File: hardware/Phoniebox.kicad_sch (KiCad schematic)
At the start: 71 parts, among them J1 GPIO, J2 Screw_Terminal_01x08, J3 Screw_Terminal_01x08, J4 Screw_Terminal_01x08, J5 Conn_01x02, J6 Conn_02x06_Odd_Even, J8 Conn_01x08, Q1 2N7002, Q2 2N7002, Q3 2N7002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

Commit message: Add OnOff-SHIM circuit to PCB
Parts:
- removed C1: 1n, Capacitor_SMD:C_0603_1608Metric_Pad1.08x0.95mm_HandSolder, symbol Device:C
- removed J5: Conn_01x02, Connector_PinHeader_2.54mm:PinHeader_1x02_P2.54mm_Vertical, symbol Connector_Generic:Conn_01x02
- removed J8: Conn_01x08, Connector_PinHeader_2.54mm:PinHeader_1x08_P2.54mm_Vertical, symbol Connector_Generic:Conn_01x08
- removed R1: 10k, Resistor_SMD:R_0603_1608Metric_Pad0.98x0.95mm_HandSolder, symbol Device:R
- removed R2: 100, Resistor_SMD:R_0603_1608Metric_Pad0.98x0.95mm_HandSolder, symbol Device:R
- added C21: 4u7, Capacitor_SMD:C_0603_1608Metric_Pad1.08x0.95mm_HandSolder, symbol Device:C
- added D1: BAT54C, Package_TO_SOT_SMD:SOT-23, symbol Diode:BAT54C
- added J7: USB_B_Micro, Connector_USB:USB_Micro-B_Amphenol_10118194_Horizontal, symbol Connector:USB_B_Micro
- added J8: Conn_02x04_Odd_Even, Connector_PinHeader_2.54mm:PinHeader_2x04_P2.54mm_Vertical_SMD, symbol Connector_Generic:Conn_02x04_Odd_Even
- added Q7: AO3401A, Package_TO_SOT_SMD:SOT-23, symbol Transistor_FET:AO3401A
- added Q8: 2N7002, Package_TO_SOT_SMD:SOT-23, symbol Transistor_FET:2N7002
- added R24: 100k, Resistor_SMD:R_0603_1608Metric_Pad0.98x0.95mm_HandSolder, symbol Device:R
- added R25: 10k, Resistor_SMD:R_0603_1608Metric_Pad0.98x0.95mm_HandSolder, symbol Device:R
- added R26, R27, R28: 1k, Resistor_SMD:R_0603_1608Metric_Pad0.98x0.95mm_HandSolder, symbol Device:R
- J6: footprint Connector_PinHeader_2.54mm:PinHeader_2x06_P2.54mm_Vertical -> Connector_PinHeader_2.54mm:PinHeader_2x06_P2.54mm_Vertical_SMD
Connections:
- net ~{MUTE} is gone; now on net GPIO2: U1.5 (~{MUTE})
- net +3V3: now also J8.1 (Pin_1), R26.2, R28.2
- net +5V: now also Q7.3 (D), R27.2
- net Button_1: now also D1.3, R25.1
- net GND: now also J4.1 (Pin_1), J4.4 (Pin_4), C21.2, J7.5 (GND), J7.6 (Shield), J8.3 (Pin_3), Q8.2 (S); no longer J4.3 (Pin_3), J4.6 (Pin_6)
- net GPIO2: no longer U1.12 (~{SHDN})
- net GPIO3: now also U1.12 (~{SHDN})
- net INL: now also J4.7 (Pin_7); no longer J4.1 (Pin_1)
- net INR: now also J4.8 (Pin_8); no longer J4.2 (Pin_2)
- net IRQ: now also J8.4 (Pin_4)
- net MISO: now also J8.5 (Pin_5)
- net MOSI: now also J8.6 (Pin_6)
- net Power_Cut: no longer J1.7 (Pin_7)
- net RST: now also J8.2 (Pin_2)
- net SCK: now also J8.7 (Pin_7)
- net SDA: now also J8.8 (Pin_8)
- net SPK_L+: now also J4.2 (Pin_2); no longer J4.4 (Pin_4)
- net SPK_L-: now also J4.3 (Pin_3); no longer J4.5 (Pin_5)
- net SPK_R+: now also J4.6 (Pin_6); no longer J4.8 (Pin_8)
- net SPK_R-: now also J4.5 (Pin_5); no longer J4.7 (Pin_7)
- net Trigger: no longer J1.11 (Pin_11)
- new net: D1.1, R27.1
- new net GPIO17_Trigger: D1.2, J1.11 (Pin_11), R28.1
- new net GPIO4_PowerOff: C21.1, J1.7 (Pin_7), Q8.1 (G), R26.1
- new net Q7_G: Q7.1 (G), Q8.3 (D), R24.1, R25.2
- new net VBUS: J7.1 (VBUS), Q7.2 (S), R24.2

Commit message: Fix DRC errors/warnings, Add round edges for PCB.
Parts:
- removed J6: Conn_02x06_Odd_Even, Connector_PinHeader_2.54mm:PinHeader_2x06_P2.54mm_Vertical_SMD, symbol Connector_Generic:Conn_02x06_Odd_Even
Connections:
- net +3V3: no longer J1.1 (Pin_1)
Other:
- note removed: "On/Off SHIM"
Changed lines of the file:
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@@
   (junction (at 130.81 81.28) (diameter 0) (color 0 0 0 0)
   )
-  (junction (at 144.78 29.21) (diameter 1.016) (color 0 0 0 0)
-  )
   (junction (at 207.01 143.51) (diameter 0) (color 0 0 0 0)
   )
@@
   (junction (at 119.38 102.87) (diameter 0) (color 0 0 0 0)
   )
-  (junction (at -78.74 21.59) (diameter 1.016) (color 0 0 0 0)
-  )
   (wire (pts (xy 411.48 135.89) (xy 420.37 135.89))
     (stroke (width 0) (type default) (color 0 0 0 0))
@@
     (stroke (width 0) (type solid) (color 0 0 0 0))
   )
-  (wire (pts (xy 144.78 31.75) (xy 142.24 31.75))
-    (stroke (width 0) (type solid) (color 0 0 0 0))
-  )
   (wire (pts (xy 252.73 25.4) (xy 273.05 25.4))
     (stroke (width 0) (type default) (color 0 0 0 0))
@@
     (stroke (width 0) (type solid) (color 0 0 0 0))
   )
-  (wire (pts (xy -78.74 17.78) (xy -78.74 21.59))
+  (wire (pts (xy -78.74 17.78) (xy -78.74 41.91))
     (stroke (width 0) (type solid) (color 0 0 0 0))
   )
-  (wire (pts (xy 111.76 36.83) (xy 129.54 36.83))
-    (stroke (width 0) (type default) (color 0 0 0 0))
-  )
   (wire (pts (xy 59.69 34.29) (xy 59.69 35.56))
     (stroke (width 0) (type default) (color 0 0 0 0))
@@
     (stroke (width 0) (type default) (color 0 0 0 0))
   )
-  (wire (pts (xy 124.46 39.37) (xy 124.46 45.72))
-    (stroke (width 0) (type default) (color 0 0 0 0))
-  )
   (wire (pts (xy -58.42 36.83) (xy -58.42 44.45))
     (stroke (width 0) (type solid) (color 0 0 0 0))
@@
     (stroke (width 0) (type default) (color 0 0 0 0))
   )
-  (wire (pts (xy 111.76 41.91) (xy 129.54 41.91))
-    (stroke (width 0) (type default) (color 0 0 0 0))
-  )
   (wire (pts (xy -58.42 17.78) (xy -58.42 21.59))
     (stroke (width 0) (type solid) (color 0 0 0 0))
@@
     (stroke (width 0) (type default) (color 0 0 0 0))
   )
-  (wire (pts (xy 142.24 34.29) (xy 144.78 34.29))
-    (stroke (width 0) (type default) (color 0 0 0 0))
-  )
   (wire (pts (xy 101.6 81.28) (xy 104.14 81.28))
     (stroke (width 0) (type default) (color 0 0 0 0))
@@
     (stroke (width 0) (type solid) (color 0 0 0 0))
   )
-  (wire (pts (xy -78.74 21.59) (xy -78.74 41.91))
-    (stroke (width 0) (type solid) (color 0 0 0 0))
-  )
   (wire (pts (xy 175.26 39.37) (xy 184.15 39.37))
     (stroke (width 0) (type default) (color 0 0 0 0))
@@
     (stroke (width 0) (type default) (color 0 0 0 0))
   )
-  (wire (pts (xy 144.78 29.21) (xy 144.78 31.75))
-    (stroke (width 0) (type solid) (color 0 0 0 0))
-  )
   (wire (pts (xy 373.38 44.45) (xy 373.38 41.91))
     (stroke (width 0) (type default) (color 0 0 0 0))
@@
     (stroke (width 0) (type default) (color 0 0 0 0))
   )
-  (wire (pts (xy 129.54 39.37) (xy 124.46 39.37))
-    (stroke (width 0) (type default) (color 0 0 0 0))
-  )
   (wire (pts (xy 153.67 101.6) (xy 153.67 102.87))
     (stroke (width 0) (type default) (color 0 0 0 0))
@@
     (stroke (width 0) (type default) (color 0 0 0 0))
   )
-  (wire (pts (xy 124.46 29.21) (xy 129.54 29.21))
-    (stroke (width 0) (type solid) (color 0 0 0 0))
-  )
   (wire (pts (xy 162.56 88.9) (xy 153.67 88.9))
     (stroke (width 0) (type default) (color 0 0 0 0))
@@
     (stroke (width 0) (type default) (color 0 0 0 0))
   )
-  (wire (pts (xy 144.78 25.4) (xy 144.78 29.21))
-    (stroke (width 0) (type solid) (color 0 0 0 0))
-  )
   (wire (pts (xy 207.01 146.05) (xy 207.01 143.51))
     (stroke (width 0) (type default) (color 0 0 0 0))
@@
     (stroke (width 0) (type default) (color 0 0 0 0))
   )
-  (wire (pts (xy 144.78 45.72) (xy 144.78 34.29))
-    (stroke (width 0) (type default) (color 0 0 0 0))
-  )
   (wire (pts (xy 403.86 135.89) (xy 401.32 135.89))
     (stroke (width 0) (type default) (color 0 0 0 0))
@@
     (stroke (width 0) (type solid) (color 0 0 0 0))
   )
-  (wire (pts (xy 144.78 29.21) (xy 142.24 29.21))
-    (stroke (width 0) (type solid) (color 0 0 0 0))
-  )
   (wire (pts (xy 219.71 27.94) (xy 231.14 27.94))
     (stroke (width 0) (type default) (color 0 0 0 0))
@@
     (stroke (width 0) (type default) (color 0 0 0 0))
   )
-  (wire (pts (xy -78.74 21.59) (xy -73.66 21.59))
-    (stroke (width 0) (type solid) (color 0 0 0 0))
-  )
   (wire (pts (xy 153.67 39.37) (xy 162.56 39.37))
     (stroke (width 0) (type default) (color 0 0 0 0))
@@
     (stroke (width 0) (type default) (color 0 0 0 0))
   )
-  (wire (pts (xy 124.46 25.4) (xy 124.46 29.21))
-    (stroke (width 0) (type solid) (color 0 0 0 0))
-  )
   (wire (pts (xy 481.33 105.41) (xy 478.79 105.41))
     (stroke (width 0) (type default) (color 0 0 0 0))
@@
     (stroke (width 0) (type default) (color 0 0 0 0))
   )
-  (text "On/Off SHIM" (at 130.81 19.05 0)
-    (effects (font (size 1.27 1.27)) (justify left bottom))
-  )
   (text "Buttons" (at 271.78 45.72 0)
     (effects (font (size 1.27 1.27)) (justify left bottom))
@@
     (effects (font (size 1.27 1.27)) (justify right bottom))
   )
-  (label "Power_Cut" (at 111.76 36.83 0)
-    (effects (font (size 1.27 1.27)) (justify left bottom))
-  )
   (label "GPIO12" (at -34.29 59.69 180)
     (effects (font (size 1.27 1.27)) (justify right bottom))
   )
-  (label "Trigger" (at 111.76 41.91 0)
-    (effects (font (size 1.27 1.27)) (justify left bottom))
-  )
   (label "LED_2" (at 453.39 105.41 0)
     (effects (font (size 1.27 1.27)) (justify left bottom))
@@
     (pin "2")
   )
-  (symbol (lib_id "power:+5V") (at 144.78 25.4 0) (unit 1)
-    (in_bom yes) (on_board yes)
-    (property "Reference" "#PWR0122" (id 0) (at 144.78 29.21 0)
-      (effects (font (size 1.27 1.27)) hide)
-    )
-    (property "Value" "+5V" (id 1) (at 145.1483 21.0756 0))
-    (property "Footprint" "" (id 2) (at 144.78 25.4 0))
-    (property "Datasheet" "" (id 3) (at 144.78 25.4 0))
-    (pin "1")
-  )
   (symbol (lib_id "Device:R") (at 115.57 135.89 180) (unit 1)
     (in_bom yes) (on_board yes) (fields_autoplaced)
@@
     (pin "1")
   )
-  (symbol (lib_id "power:+3.3V") (at 124.46 25.4 0) (unit 1)
-    (in_bom yes) (on_board yes)
-    (property "Reference" "#PWR0120" (id 0) (at 124.46 29.21 0)
-      (effects (font (size 1.27 1.27)) hide)
-    )
-    (property "Value" "+3.3V" (id 1) (at 124.8283 21.0756 0))
-    (property "Footprint" "" (id 2) (at 124.46 25.4 0))
-    (property "Datasheet" "" (id 3) (at 124.46 25.4 0))
-    (pin "1")
-  )
   (symbol (lib_id "power:+3.3VA") (at 358.14 41.91 0) (unit 1)
     (in_bom yes) (on_board yes) (fields_autoplaced)
@@
     (pin "1")
   )
-  (symbol (lib_id "Connector_Generic:Conn_02x06_Odd_Even") (at 134.62 34.29 0) (unit 1)
-    (in_bom yes) (on_board yes) (fields_autoplaced)
-    (property "Reference" "J6" (id 0) (at 135.89 25.4 0))
-    (property "Value" "Conn_02x06_Odd_Even" (id 1) (at 135.89 25.4 0)
-      (effects (font (size 1.27 1.27)) hide)
-    )
-    (property "Footprint" "Connector_PinHeader_2.54mm:PinHeader_2x06_P2.54mm_Vertical_SMD" (id 2) (at 134.62 34.29 0)
-      (effects (font (size 1.27 1.27)) hide)
-    )
-    (property "Datasheet" "~" (id 3) (at 134.62 34.29 0)
-      (effects (font (size 1.27 1.27)) hide)
-    )
-    (pin "1")
-    (pin "10")
-    (pin "11")
-    (pin "12")
-    (pin "2")
-    (pin "3")
-    (pin "4")
-    (pin "5")
-    (pin "6")
-    (pin "7")
-    (pin "8")
-    (pin "9")
-  )
   (symbol (lib_id "power:+5V") (at 313.69 15.24 0) (unit 1)
     (in_bom yes) (on_board yes)
@@
     (pin "1")
   )
-  (symbol (lib_id "power:GND") (at 144.78 45.72 0) (unit 1)
-    (in_bom yes) (on_board yes)
-    (property "Reference" "#PWR0124" (id 0) (at 144.78 52.07 0)
-      (effects (font (size 1.27 1.27)) hide)
-    )
-    (property "Value" "GND" (id 1) (at 144.8943 50.0444 0))
-    (property "Footprint" "" (id 2) (at 144.78 45.72 0))
-    (property "Datasheet" "" (id 3) (at 144.78 45.72 0))
-    (pin "1")
-  )
   (symbol (lib_id "power:GND") (at 401.32 152.4 0) (unit 1)
     (in_bom yes) (on_board yes)
@@
     (pin "2")
   )
-  (symbol (lib_id "power:GND") (at 124.46 45.72 0) (unit 1)
-    (in_bom yes) (on_board yes)
-    (property "Reference" "#PWR0123" (id 0) (at 124.46 52.07 0)
-      (effects (font (size 1.27 1.27)) hide)
-    )
-    (property "Value" "GND" (id 1) (at 124.5743 50.0444 0))
-    (property "Footprint" "" (id 2) (at 124.46 45.72 0))
-    (property "Datasheet" "" (id 3) (at 124.46 45.72 0))
-    (pin "1")
-  )
   (symbol (lib_id "power:GND") (at 401.32 121.92 0) (unit 1)
     (in_bom yes) (on_board yes)
@@
       (reference "#PWR0119") (unit 1) (value "+3.3V") (footprint "")
     )
-    (path "/4b08ea74-839c-4011-a075-b08e2ab717fe"
-      (reference "#PWR0120") (unit 1) (value "+3.3V") (footprint "")
-    )
     (path "/baf3a49f-9dbb-4b6b-8377-296dfb4e70c7"
       (reference "#PWR0121") (unit 1) (value "GND") (footprint "")
     )
-    (path "/402268e3-d531-4d65-ae41-9da869734677"
-      (reference "#PWR0122") (unit 1) (value "+5V") (footprint "")
-    )
-    (path "/b84a0fa1-824d-4c2d-8864-5ad39f5e3539"
-      (reference "#PWR0123") (unit 1) (value "GND") (footprint "")
-    )
-    (path "/99306b7b-532d-48e8-9e09-6b18c8178118"
-      (reference "#PWR0124") (unit 1) (value "GND") (footprint "")
-    )
     (path "/d96e2a38-9296-45c5-bcd1-66b1165ebb7d"
       (reference "#PWR0125") (unit 1) (value "+3.3V") (footprint "")
@@
       (reference "J4") (unit 1) (value "Screw_Terminal_01x08") (footprint "TerminalBlock_Phoenix:TerminalBlock_Phoenix_MPT-0,5-8-2.54_1x08_P2.54mm_Horizontal")
     )
-    (path "/67ddacc1-ad12-4524-9b37-d777c6826f94"
-      (reference "J6") (unit 1) (value "Conn_02x06_Odd_Even") (footprint "Connector_PinHeader_2.54mm:PinHeader_2x06_P2.54mm_Vertical_SMD")
-    )
     (path "/d8d884ee-743c-4ab0-8419-a234428ecfd5"

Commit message: Create hierachical schematic sheets for audio/LED/buttons.
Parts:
- removed C10, C11, C12, C13: 220p, Capacitor_SMD:C_0603_1608Metric_Pad1.08x0.95mm_HandSolder, symbol Device:C
- removed C14, C15, C16, C8, C9: 1n, Capacitor_SMD:C_0603_1608Metric_Pad1.08x0.95mm_HandSolder, symbol Device:C
- removed C17, C20, C22: 100n, Capacitor_SMD:C_0603_1608Metric_Pad1.08x0.95mm_HandSolder, symbol Device:C
- removed C18, C19, C23, C26, C4, C7: 10u, Capacitor_SMD:C_1210_3225Metric_Pad1.33x2.70mm_HandSolder, symbol Device:C
- removed C2, C3, C5, C6: 1u, Capacitor_SMD:C_0603_1608Metric_Pad1.08x0.95mm_HandSolder, symbol Device:C
- removed C24, C25: 2u2, Capacitor_SMD:C_0603_1608Metric_Pad1.08x0.95mm_HandSolder, symbol Device:C
- removed C27, C28: 2n2, Capacitor_SMD:C_0603_1608Metric_Pad1.08x0.95mm_HandSolder, symbol Device:C
- removed FB1, FB2, FB3, FB4: FerriteBead_Small, Resistor_SMD:R_0603_1608Metric_Pad0.98x0.95mm_HandSolder, symbol Device:FerriteBead_Small
- removed Q1, Q2, Q3, Q4, Q5, Q6: 2N7002, Package_TO_SOT_SMD:SOT-23, symbol Transistor_FET:2N7002
- removed R10, R12, R20, R3, R4, R6, R8: 10k, Resistor_SMD:R_0603_1608Metric_Pad0.98x0.95mm_HandSolder, symbol Device:R
- removed R11, R13, R14, R15, R16, R17, R18, R19, R21, R7, R9: 100, Resistor_SMD:R_0603_1608Metric_Pad0.98x0.95mm_HandSolder, symbol Device:R
- removed R22, R23: 470, Resistor_SMD:R_0603_1608Metric_Pad0.98x0.95mm_HandSolder, symbol Device:R
- removed R5: 10, Resistor_SMD:R_0603_1608Metric_Pad0.98x0.95mm_HandSolder, symbol Device:R
- removed U1: PAM8406, Package_SO:SOP-16_3.9x9.9mm_P1.27mm, symbol Phoniebox:PAM8406
- removed U2: TPS79333-EP, Package_TO_SOT_SMD:SOT-23-5, symbol Regulator_Linear:TPS79333-EP
- removed U3: PCM5102, Package_SO:TSSOP-20_4.4x6.5mm_P0.65mm, symbol Audio:PCM5102
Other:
- added sheet Audio (audio.kicad_sch)
- added sheet Buttons (buttons.kicad_sch)
- moved on the sheet: J2, J3, J4

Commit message: Place OnOffSHIM circuit on separate page.
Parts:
- removed C21: 4u7, Capacitor_SMD:C_0603_1608Metric_Pad1.08x0.95mm_HandSolder, symbol Device:C
- removed D1: BAT54C, Package_TO_SOT_SMD:SOT-23, symbol Diode:BAT54C
- removed Q7: AO3401A, Package_TO_SOT_SMD:SOT-23, symbol Transistor_FET:AO3401A
- removed Q8: 2N7002, Package_TO_SOT_SMD:SOT-23, symbol Transistor_FET:2N7002
- removed R24: 100k, Resistor_SMD:R_0603_1608Metric_Pad0.98x0.95mm_HandSolder, symbol Device:R
- removed R25: 10k, Resistor_SMD:R_0603_1608Metric_Pad0.98x0.95mm_HandSolder, symbol Device:R
- removed R26, R27, R28: 1k, Resistor_SMD:R_0603_1608Metric_Pad0.98x0.95mm_HandSolder, symbol Device:R
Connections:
- net VBUS renamed OnOffSHIM/VBUS
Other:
- added sheet OnOffSHIM (onoffschim.kicad_sch)
- note added: "Connector for RFID-RC522 PCB"
- note added: "PI HAT EEPROM"
- note added: "Raspberry PI 40-pin header"
- note removed: "RC522"
- moved on the sheet: J1, J2, J3, J4, J7, J8, U4

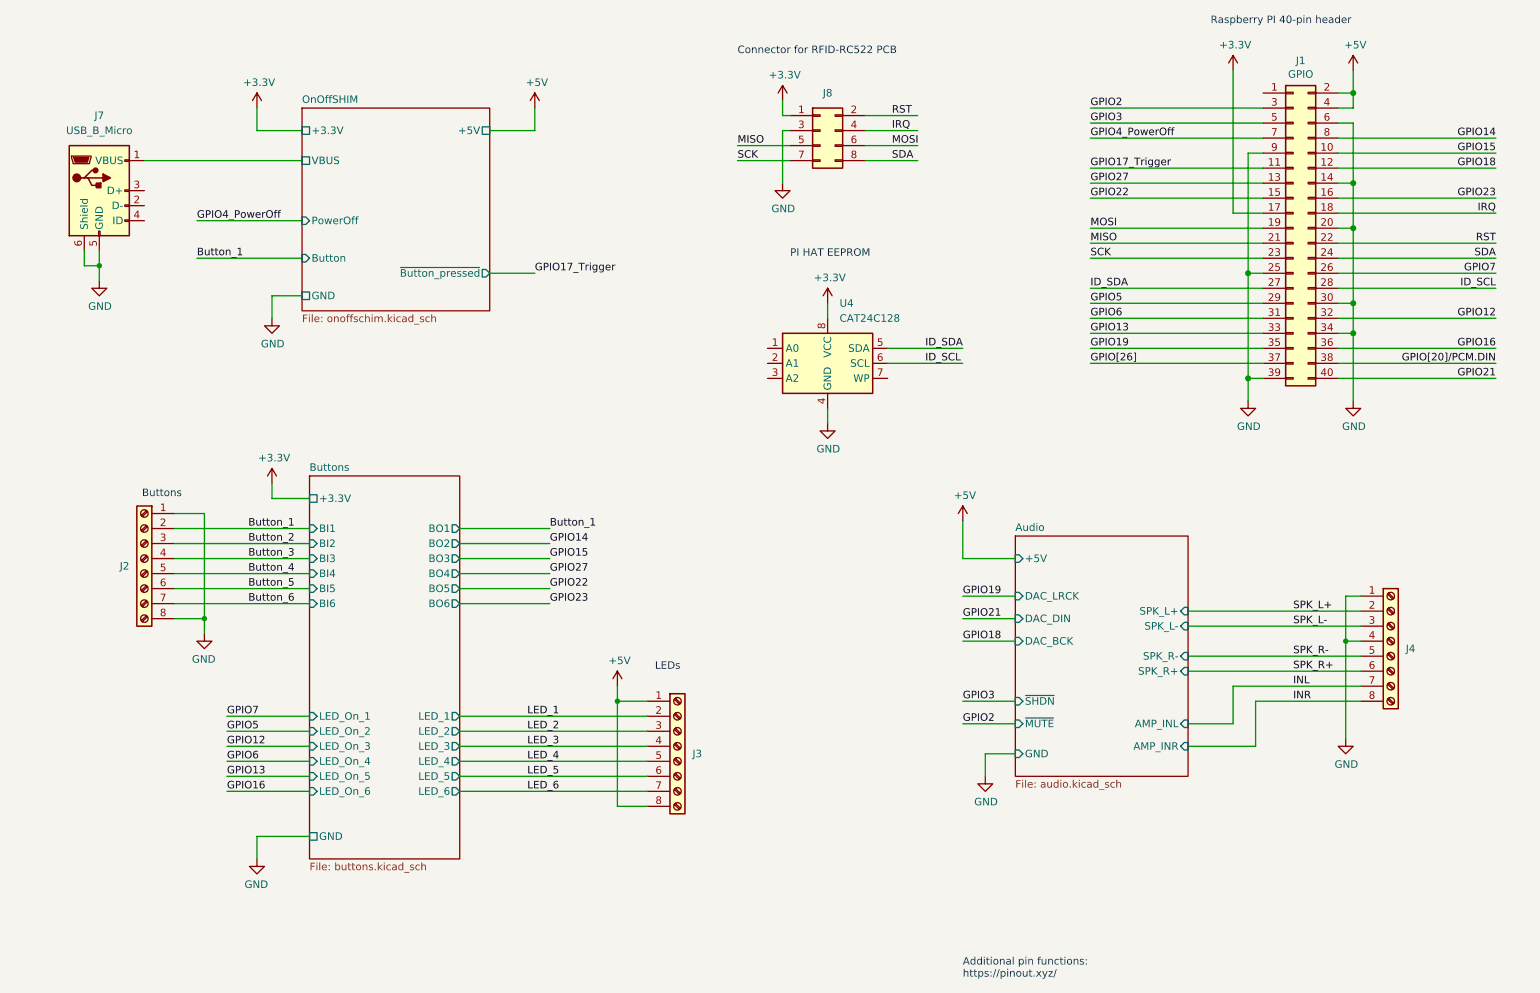
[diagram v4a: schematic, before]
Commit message: Add I2C header for displays. Mute/SHDN now controlled by previously unused GPIO20/26. LED1 is now hardwired to ON=V3P3 high. GPIO7 would still be available to control LED1. Change debounce circuit to have both directions up/down debounced. Use resistor/capacitor values to debounce button press times <100ms.
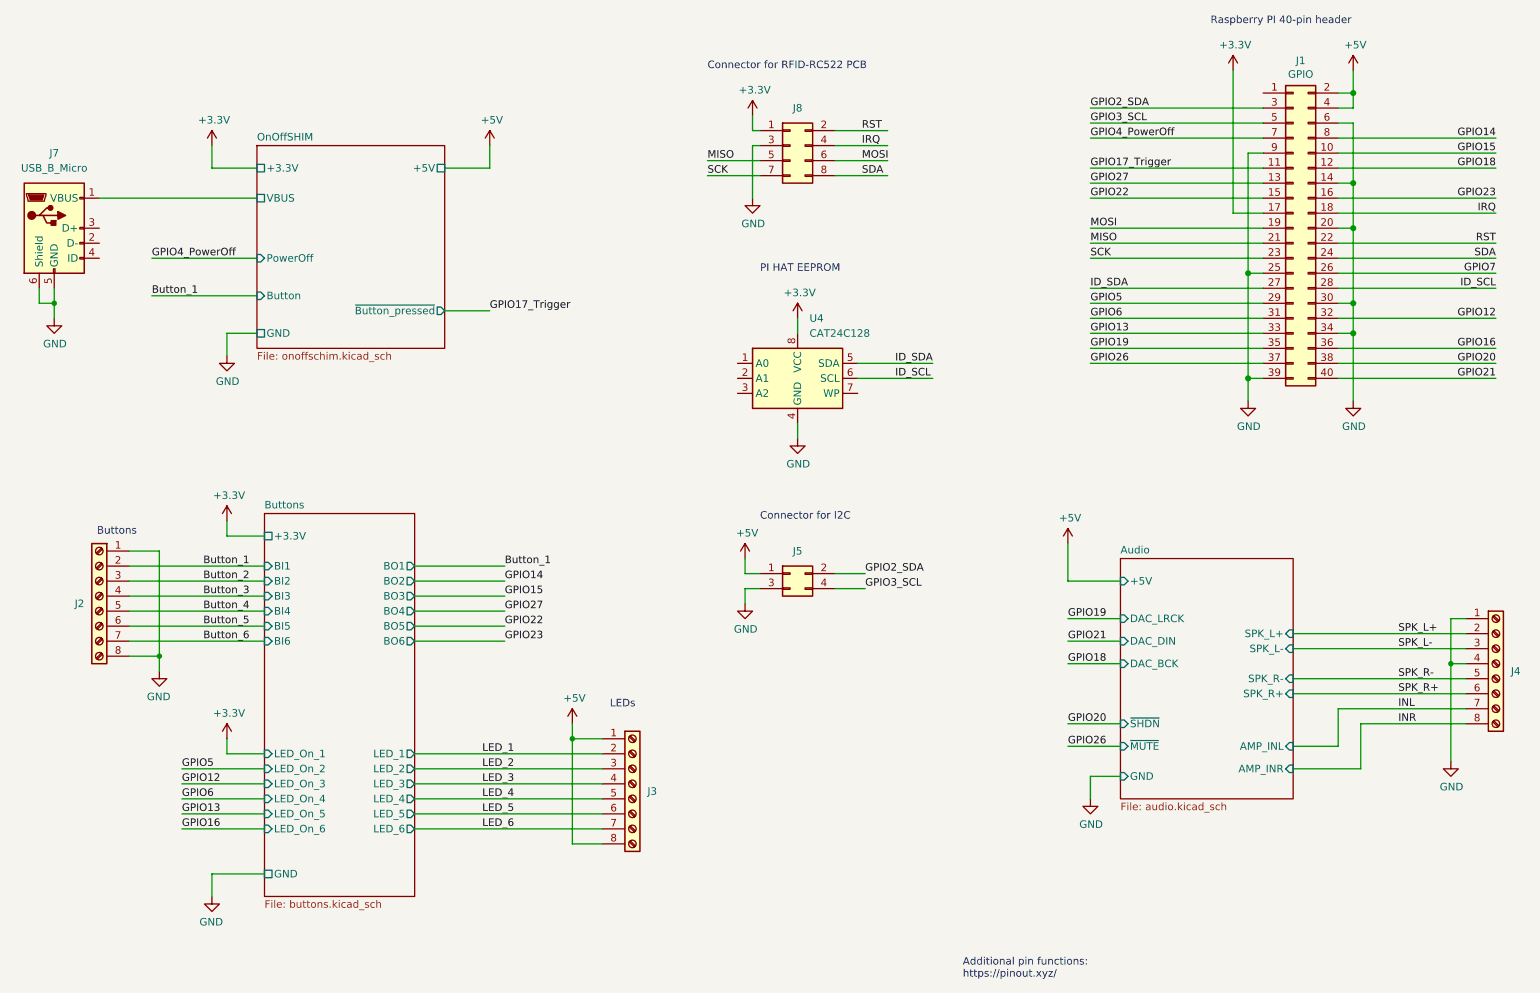
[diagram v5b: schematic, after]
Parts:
- added J5: Conn_02x02_Odd_Even, Connector_PinHeader_2.54mm:PinHeader_2x02_P2.54mm_Vertical_SMD, symbol Connector_Generic:Conn_02x02_Odd_Even
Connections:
- net +5V: now also J5.1 (Pin_1)
- net GND: now also J5.3 (Pin_3)
- net GPIO2 renamed GPIO2_SDA
- net GPIO2_SDA: now also J5.2 (Pin_2)
- net GPIO3 renamed GPIO3_SCL
- net GPIO3_SCL: now also J5.4 (Pin_4)
- net GPIO[20]/PCM.DIN renamed GPIO20
- net GPIO[26] renamed GPIO26
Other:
- note added: "Connector for I2C"
- moved on the sheet: J2, J3, J4, J7, J8, U4
